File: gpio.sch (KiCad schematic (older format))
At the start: 5 parts, among them J1 CONN_02X20, J2 CONN_02X20, U1 LFE5U-25F-6BG381C

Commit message: analog: audio ring2 resistor DAC network connected to FPGA copper infill is getting thin, so minimal-thickness traces are used 0.127 mm
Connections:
- net labels added: AUDIO_V0, AUDIO_V1, AUDIO_V2, AUDIO_V3
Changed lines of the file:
@@
 Text Notes 7050 5750 0    60   ~ 0
 J2_5-J2_23 connected to  BANK2,3 on "ram" sheet\nJ2_25-J2_35 connected to BANK1 on "gpdi" sheet
+Text GLabel 4200 2500 0    60   Input ~ 0
+SW0
 Text GLabel 5700 2500 2    60   Input ~ 0
-SW0
+SW1
 Text GLabel 5700 2700 2    60   Input ~ 0
-SW1
-Text GLabel 4200 2500 0    60   Input ~ 0
 SW2
 Text GLabel 4200 2700 0    60   Input ~ 0
 SW3
+Text GLabel 4150 5250 0    60   Input ~ 0
+AUDIO_V3
+Text GLabel 5650 4650 2    60   Input ~ 0
+AUDIO_V2
+Text GLabel 4150 4650 0    60   Input ~ 0
+AUDIO_V1
+Text GLabel 4200 2800 0    60   Input ~ 0
+AUDIO_V0
 $EndSCHEMATC

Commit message: move one audio-v pin from bank0 to bank7 so now all audio jack pins are on bank7
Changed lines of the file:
@@
 Text GLabel 4150 5250 0    60   Input ~ 0
 AUDIO_V3
+Text GLabel 4150 5450 0    60   Input ~ 0
+AUDIO_V2
 Text GLabel 5650 4650 2    60   Input ~ 0
-AUDIO_V2
+AUDIO_V1
 Text GLabel 4150 4650 0    60   Input ~ 0
-AUDIO_V1
-Text GLabel 4200 2800 0    60   Input ~ 0
 AUDIO_V0
 $EndSCHEMATC

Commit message: changing to 45F which is production device now schem symbol 45F fixed typo T8->T7 (GND) and SERDES
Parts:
- removed U1: LFE5U-25F-6BG381C, lfe5bg381:BGA-381_pitch0.8mm_dia0.4mm, symbol LFE5U-25F-6BG381C-RESCUE-ulx3s
- added U1: LFE5U-45F-6BG381C, symbol LFE5U-45F-6BG381C
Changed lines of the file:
@@
 Text GLabel 4200 2600 0    60   Input ~ 0
 J1_17+
-$Comp
-L LFE5U-25F-6BG381C-RESCUE-ulx3s U1
-U 1 1 58F23D91
-P 4950 2500
-AR Path="/58F23D91" Ref="U1"  Part="1"
-AR Path="/56AC389C/58F23D91" Ref="U1"  Part="1"
-F 0 "U1" H 4950 3450 60  0000 C CNN
-F 1 "LFE5U-25F-6BG381C" H 4950 3350 60  0000 C CNN
-F 2 "lfe5bg381:BGA-381_pitch0.8mm_dia0.4mm" H 3900 3450 60  0001 C CNN
-F 3 "" H 3900 3450 60  0000 C CNN
-	1    4950 2500
-	1    0    0    -1
-$EndComp
-$Comp
-L LFE5U-25F-6BG381C-RESCUE-ulx3s U1
-U 6 1 58F23E5F
-P 4900 4750
-AR Path="/58F23E5F" Ref="U1"  Part="6"
-AR Path="/56AC389C/58F23E5F" Ref="U1"  Part="6"
-F 0 "U1" H 4900 5700 60  0000 C CNN
-F 1 "LFE5U-25F-6BG381C" H 4900 5600 60  0000 C CNN
-F 2 "lfe5bg381:BGA-381_pitch0.8mm_dia0.4mm" H 3850 5700 60  0001 C CNN
-F 3 "" H 3850 5700 60  0000 C CNN
-	6    4900 4750
-	1    0    0    -1
-$EndComp
 Text GLabel 5700 1800 2    60   Input ~ 0
 J1_5-
@@
 Text GLabel 4150 4650 0    60   Input ~ 0
 AUDIO_V0
+$Comp
+L LFE5U-45F-6BG381C U1
+U 1 1 5A0782EF
+P 4950 2500
+F 0 "U1" H 4950 3450 60  0000 C CNN
+F 1 "LFE5U-45F-6BG381C" H 4950 3350 60  0000 C CNN
+F 2 "" H 3900 3450 60  0000 C CNN
+F 3 "" H 3900 3450 60  0000 C CNN
+	1    4950 2500
+	1    0    0    -1
+$EndComp
+$Comp
+L LFE5U-45F-6BG381C U1
+U 6 1 5A0783C9
+P 4900 4750
+F 0 "U1" H 4900 5700 60  0000 C CNN
+F 1 "LFE5U-45F-6BG381C" H 4900 5600 60  0000 C CNN
+F 2 "" H 3850 5700 60  0000 C CNN
+F 3 "" H 3850 5700 60  0000 C CNN
+	6    4900 4750
+	1    0    0    -1
+$EndComp
 $EndSCHEMATC

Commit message: open-close to check that everything loads fine
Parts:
- U1: symbol LFE5U-45F-6BG381C -> LFE5U-45F-6BG381C-RESCUE-ulx3s
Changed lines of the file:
@@
 AUDIO_V0
 $Comp
+L LFE5U-45F-6BG381C-RESCUE-ulx3s U1
+U 6 1 5A0783C9
+P 4900 4750
+AR Path="/5A0783C9" Ref="U1"  Part="6"
+AR Path="/56AC389C/5A0783C9" Ref="U1"  Part="6"
+F 0 "U1" H 4900 5700 60  0000 C CNN
+F 1 "LFE5U-45F-6BG381C" H 4900 5600 60  0000 C CNN
+F 2 "" H 3850 5700 60  0000 C CNN
+F 3 "" H 3850 5700 60  0000 C CNN
+	6    4900 4750
+	1    0    0    -1
+$EndComp
+$Comp
 L LFE5U-45F-6BG381C U1
-U 1 1 5A0782EF
+U 1 1 5A0737C6
 P 4950 2500
 F 0 "U1" H 4950 3450 60  0000 C CNN
@@
 	1    0    0    -1
 $EndComp
-$Comp
-L LFE5U-45F-6BG381C U1
-U 6 1 5A0783C9
-P 4900 4750
-F 0 "U1" H 4900 5700 60  0000 C CNN
-F 1 "LFE5U-45F-6BG381C" H 4900 5600 60  0000 C CNN
-F 2 "" H 3850 5700 60  0000 C CNN
-F 3 "" H 3850 5700 60  0000 C CNN
-	6    4900 4750
-	1    0    0    -1
-$EndComp

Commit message: connected missing SD card pins to esp-32
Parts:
- U1: footprint (none) -> lfe5bg381:BGA-381_pitch0.8mm_dia0.4mm
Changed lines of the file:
@@
 F 0 "U1" H 4900 5700 60  0000 C CNN
 F 1 "LFE5U-45F-6BG381C" H 4900 5600 60  0000 C CNN
-F 2 "" H 3850 5700 60  0000 C CNN
+F 2 "lfe5bg381:BGA-381_pitch0.8mm_dia0.4mm" H 3850 5700 60  0001 C CNN
 F 3 "" H 3850 5700 60  0000 C CNN
 	6    4900 4750
@@
 F 0 "U1" H 4950 3450 60  0000 C CNN
 F 1 "LFE5U-45F-6BG381C" H 4950 3350 60  0000 C CNN
-F 2 "" H 3900 3450 60  0000 C CNN
+F 2 "lfe5bg381:BGA-381_pitch0.8mm_dia0.4mm" H 3900 3450 60  0001 C CNN
 F 3 "" H 3900 3450 60  0000 C CNN
 	1    4950 2500

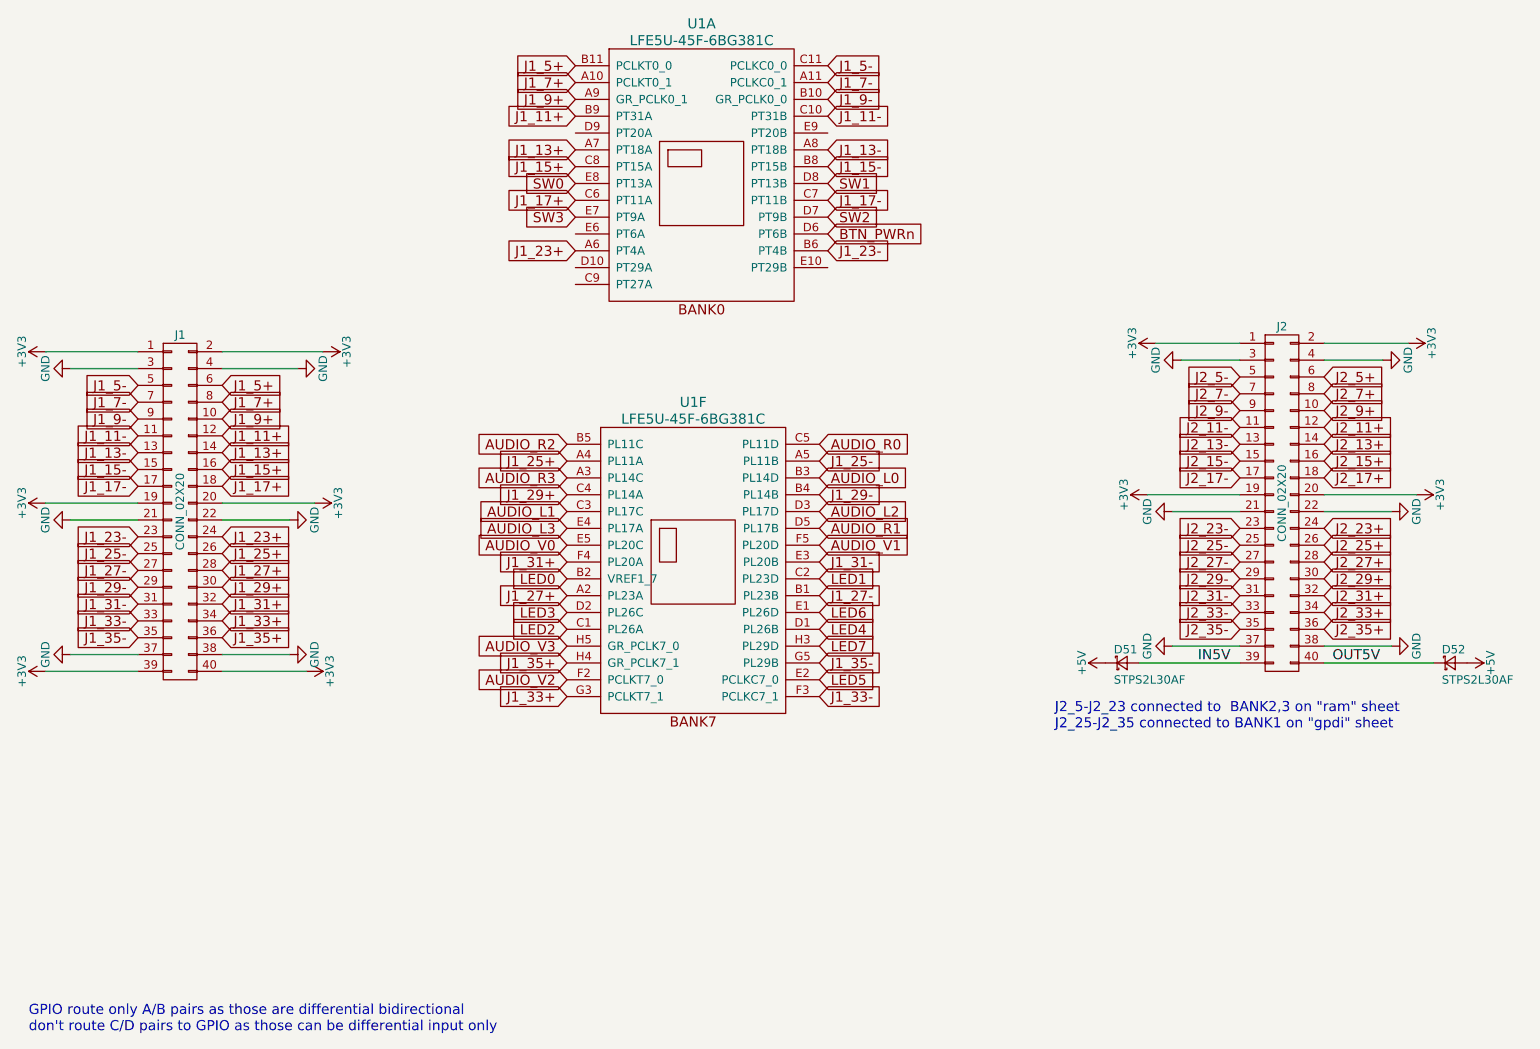
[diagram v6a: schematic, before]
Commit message: schematics: text labels that enumerate differential pairs on 2.54mm connector
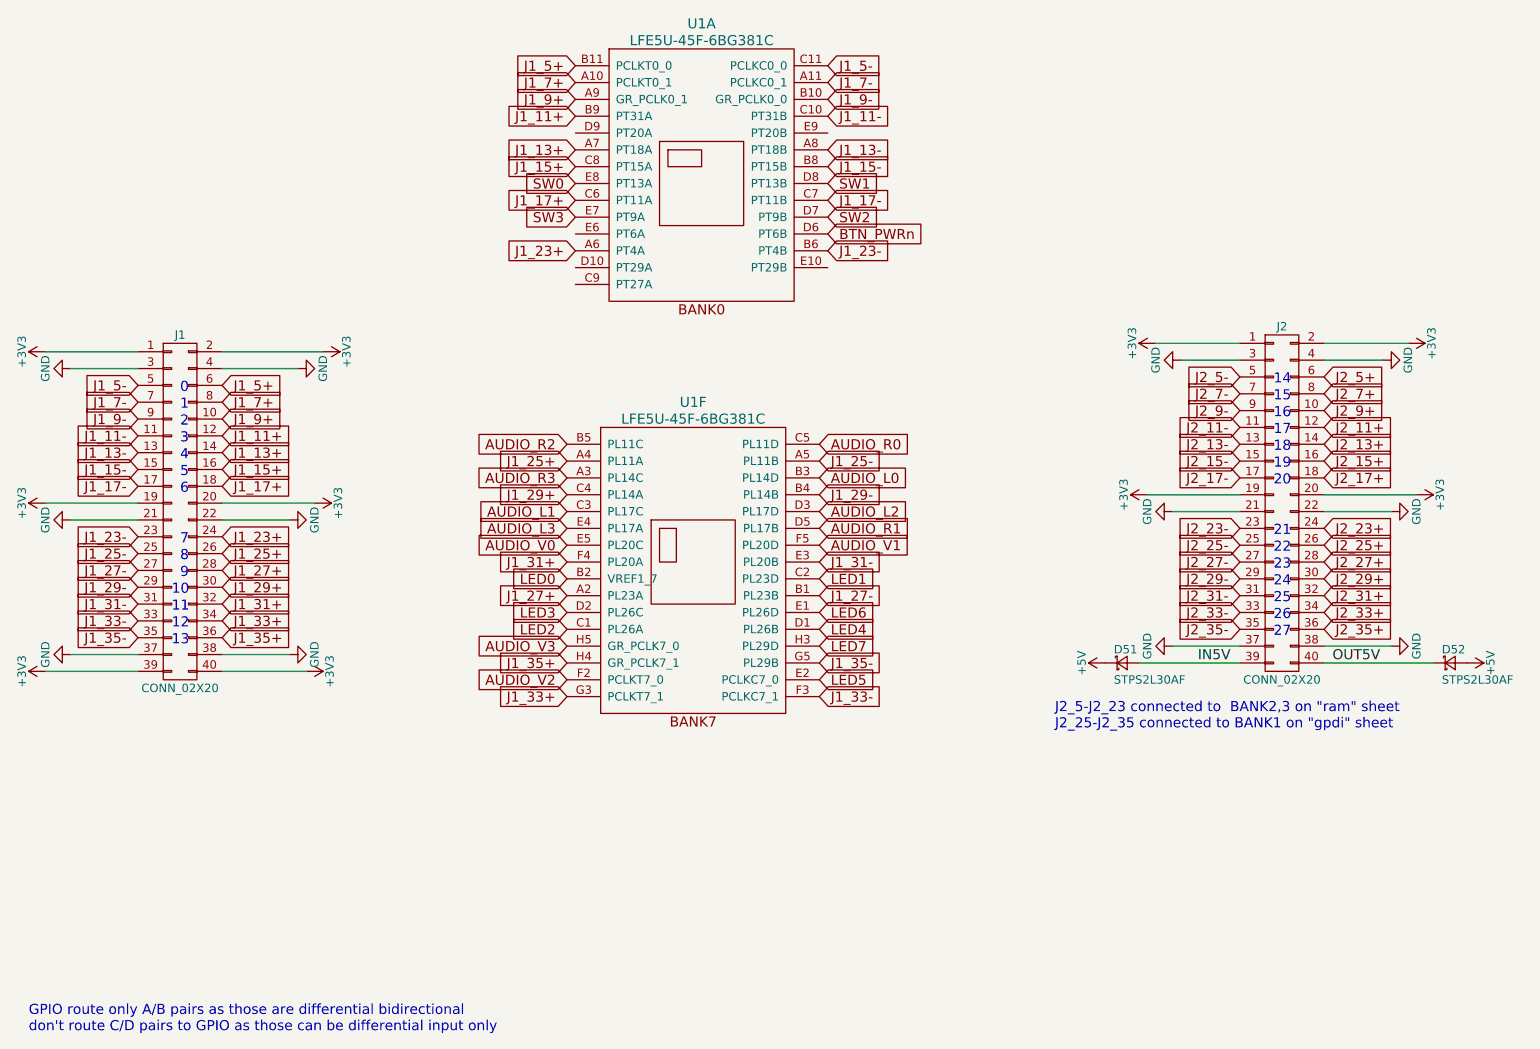
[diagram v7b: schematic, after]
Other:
- note added: "0"
- note added: "1"
- note added: "10"
- note added: "11"
- note added: "12"
- note added: "13"
- note added: "14"
- note added: "15"
- note added: "16"
- note added: "17"
- note added: "18"
- note added: "19"
- note added: "2"
- note added: "20"
- note added: "21"
- note added: "22"
- note added: "23"
- note added: "24"
- note added: "25"
- note added: "26"
- note added: "27"
- note added: "3"
- note added: "4"
- note added: "5"
- note added: "6"
- note added: "7"
- note added: "8"
- note added: "9"
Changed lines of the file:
@@
 P 8400 4400
 F 0 "J2" H 8400 5450 50  0000 C CNN
-F 1 "CONN_02X20" V 8400 4400 50  0000 C CNN
+F 1 "CONN_02X20" H 8400 3350 50  0000 C CNN
 F 2 "Socket_Strips:Socket_Strip_Angled_2x20" H 8400 3450 50  0001 C CNN
 F 3 "" H 8400 3450 50  0000 C CNN
@@
 P 1850 4450
 F 0 "J1" H 1850 5500 50  0000 C CNN
-F 1 "CONN_02X20" V 1850 4450 50  0000 C CNN
+F 1 "CONN_02X20" H 1850 3400 50  0000 C CNN
 F 2 "Socket_Strips:Socket_Strip_Angled_2x20" H 1850 3500 50  0001 C CNN
 F 3 "" H 1850 3500 50  0000 C CNN
@@
 	1    0    0    -1
 $EndComp
+Text Notes 1850 3750 0    60   ~ 0
+0
+Text Notes 1850 3850 0    60   ~ 0
+1
+Text Notes 1850 3950 0    60   ~ 0
+2
+Text Notes 1850 4050 0    60   ~ 0
+3
+Text Notes 1800 4950 0    60   ~ 0
+10
+Text Notes 1850 4150 0    60   ~ 0
+4
+Text Notes 1850 4250 0    60   ~ 0
+5
+Text Notes 1850 4350 0    60   ~ 0
+6
+Text Notes 1850 4650 0    60   ~ 0
+7
+Text Notes 1850 4750 0    60   ~ 0
+8
+Text Notes 1850 4850 0    60   ~ 0
+9
+Text Notes 1800 5050 0    60   ~ 0
+11
+Text Notes 1800 5150 0    60   ~ 0
+12
+Text Notes 1800 5250 0    60   ~ 0
+13
+Text Notes 8350 3700 0    60   ~ 0
+14
+Text Notes 8350 3800 0    60   ~ 0
+15
+Text Notes 8350 3900 0    60   ~ 0
+16
+Text Notes 8350 4000 0    60   ~ 0
+17
+Text Notes 8350 4100 0    60   ~ 0
+18
+Text Notes 8350 4200 0    60   ~ 0
+19
+Text Notes 8350 4300 0    60   ~ 0
+20
+Text Notes 8350 4600 0    60   ~ 0
+21
+Text Notes 8350 4700 0    60   ~ 0
+22
+Text Notes 8350 4800 0    60   ~ 0
+23
+Text Notes 8350 4900 0    60   ~ 0
+24
+Text Notes 8350 5000 0    60   ~ 0
+25
+Text Notes 8350 5100 0    60   ~ 0
+26
+Text Notes 8350 5200 0    60   ~ 0
+27
 $EndSCHEMATC

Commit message: schematics: part numbers and URLs of datasheets and manufacturers of most chips and connectors. Small parts not done yet.
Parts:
- U1: Distributor1_URL (none) -> www.mouser.com
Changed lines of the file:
@@
 F 1 "LFE5U-45F-6BG381C" H 4900 5600 60  0000 C CNN
 F 2 "lfe5bg381:BGA-381_pitch0.8mm_dia0.4mm" H 3850 5700 60  0001 C CNN
-F 3 "" H 3850 5700 60  0000 C CNN
+F 3 "http://www.latticesemi.com/~/media/LatticeSemi/Documents/DataSheets/ECP5/FPGA-DS-02012.pdf" H 3850 5700 60  0001 C CNN
+F 4 "www.mouser.com" H 4900 4750 60  0001 C CNN "Distributor1_URL"
 	6    4900 4750
 	1    0    0    -1
@@
 F 1 "LFE5U-45F-6BG381C" H 4950 3350 60  0000 C CNN
 F 2 "lfe5bg381:BGA-381_pitch0.8mm_dia0.4mm" H 3900 3450 60  0001 C CNN
-F 3 "" H 3900 3450 60  0000 C CNN
+F 3 "http://www.latticesemi.com/~/media/LatticeSemi/Documents/DataSheets/ECP5/FPGA-DS-02012.pdf" H 3900 3450 60  0001 C CNN
+F 4 "www.mouser.com" H 4950 2500 60  0001 C CNN "Distributor1_URL"
 	1    4950 2500
 	1    0    0    -1
